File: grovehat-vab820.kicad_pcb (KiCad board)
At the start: 2 copper layers, 40 x 21 mm, 7 parts, among them P1 CONN_10X2, P2 GROVE, P3 GROVE, P4 GROVE, P5 GROVE

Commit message: adjust silkscreen
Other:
- board text added: "Designed in Taiwan"
- board text added: "moonpunch.org"
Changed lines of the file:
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@@
     (area 195.886934 143.949999 240.050001 165.050001)
     (thickness 1.6)
-    (drawings 38)
+    (drawings 40)
     (tracks 72)
     (zones 0)
@@
       (xy 3.96748 0.20574)) (layer B.SilkS) (width 0.00254))
   )
+  (gr_text "Designed in Taiwan" (at 231.5 162.9) (layer B.SilkS)
+    (effects (font (size 1 1) (thickness 0.2)) (justify mirror))
+  )
+  (gr_text moonpunch.org (at 207.8 162.9) (layer B.SilkS)
+    (effects (font (size 1 1) (thickness 0.2)) (justify mirror))
+  )
   (gr_text "CERN OHL 1.2" (at 221.8 152.6) (layer B.SilkS)

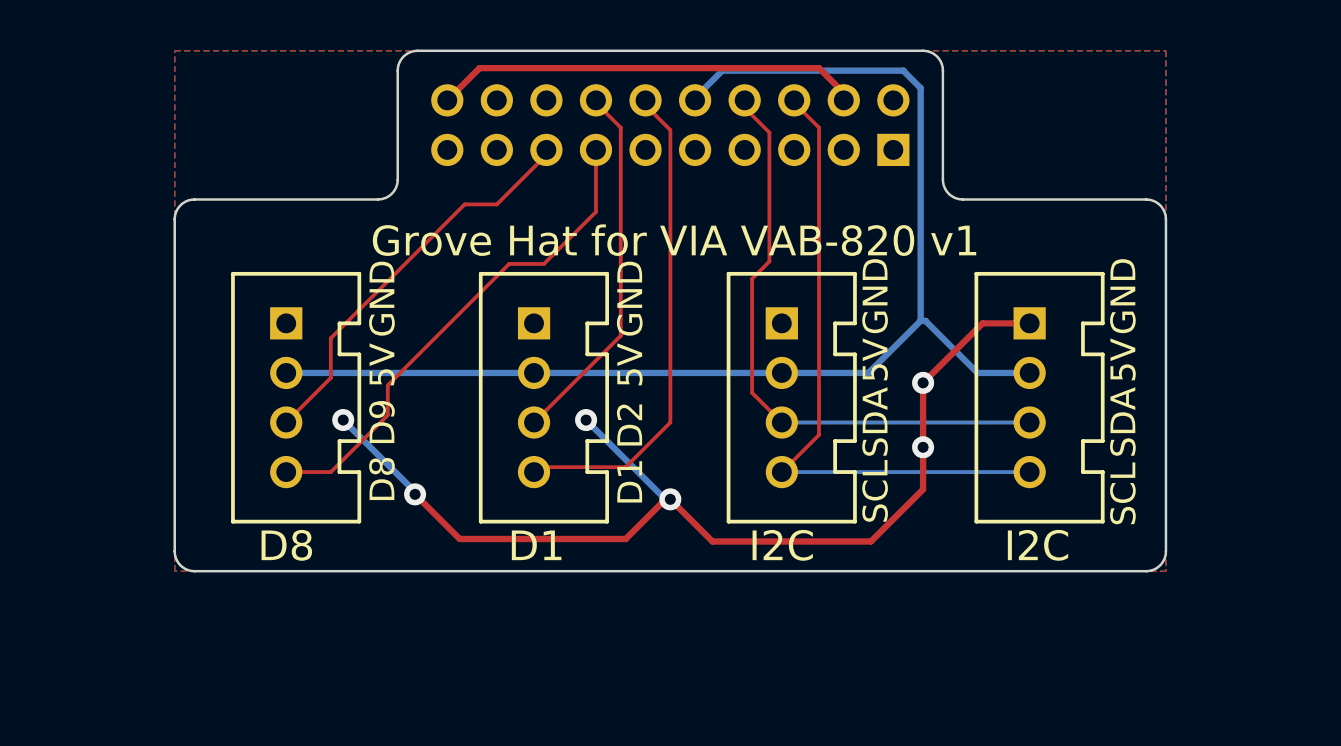
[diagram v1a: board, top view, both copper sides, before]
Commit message: updated PCB design, larger area, more spacious
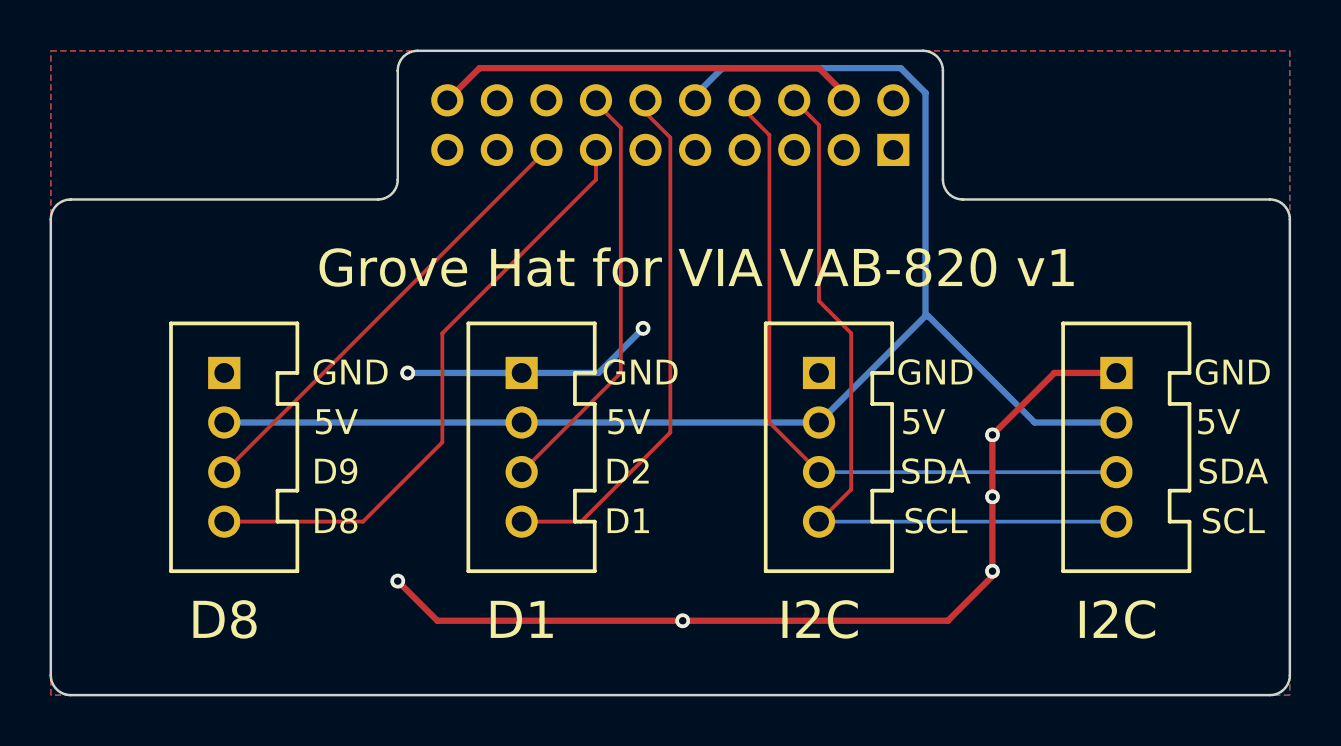
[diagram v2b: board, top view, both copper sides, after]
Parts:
- moved G*** 22.0 mm to (211.9, 166.6)
- moved G*** 11.5 mm to (218.8, 152.6)
- moved P3 4.03 mm to (238.0, 160.0)
- moved P5 3.20 mm to (202.0, 160.0)
- moved P2 2.50 mm to (226.0, 160.0)
- moved P4 2.06 mm to (214.0, 160.0)
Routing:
- net +5V: track 51.1 -> 58.9 mm
- net GND: track 59.3 -> 64.6 mm, vias 6 -> 7
- net /SCL: track 26.0 -> 30.5 mm
- net /D8: track 20.1 -> 24.5 mm
- net /SDA: track 24.2 -> 28.2 mm
- net /D9: track 16.1 -> 18.4 mm
- net /D2: track 14.9 -> 17.1 mm
- net /D1: track 19.7 -> 21.3 mm
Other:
- board size 40 x 21 mm -> 50 x 26 mm
- net class Default: via_dia 0.889 -> 0.6; via_drill 0.635 -> 0.4
